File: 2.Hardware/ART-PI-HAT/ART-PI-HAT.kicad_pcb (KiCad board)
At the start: 2 copper layers, 85 x 56 mm, 29 parts, among them J1 Conn_02x20_Odd_Even, J2 Conn_02x20_Odd_Even, J3 GC9A01, U1 XC6206_1.8V, U2 MAX30102, U3 MPU-6050, U4 GP-02, U5 IPEX_CONN

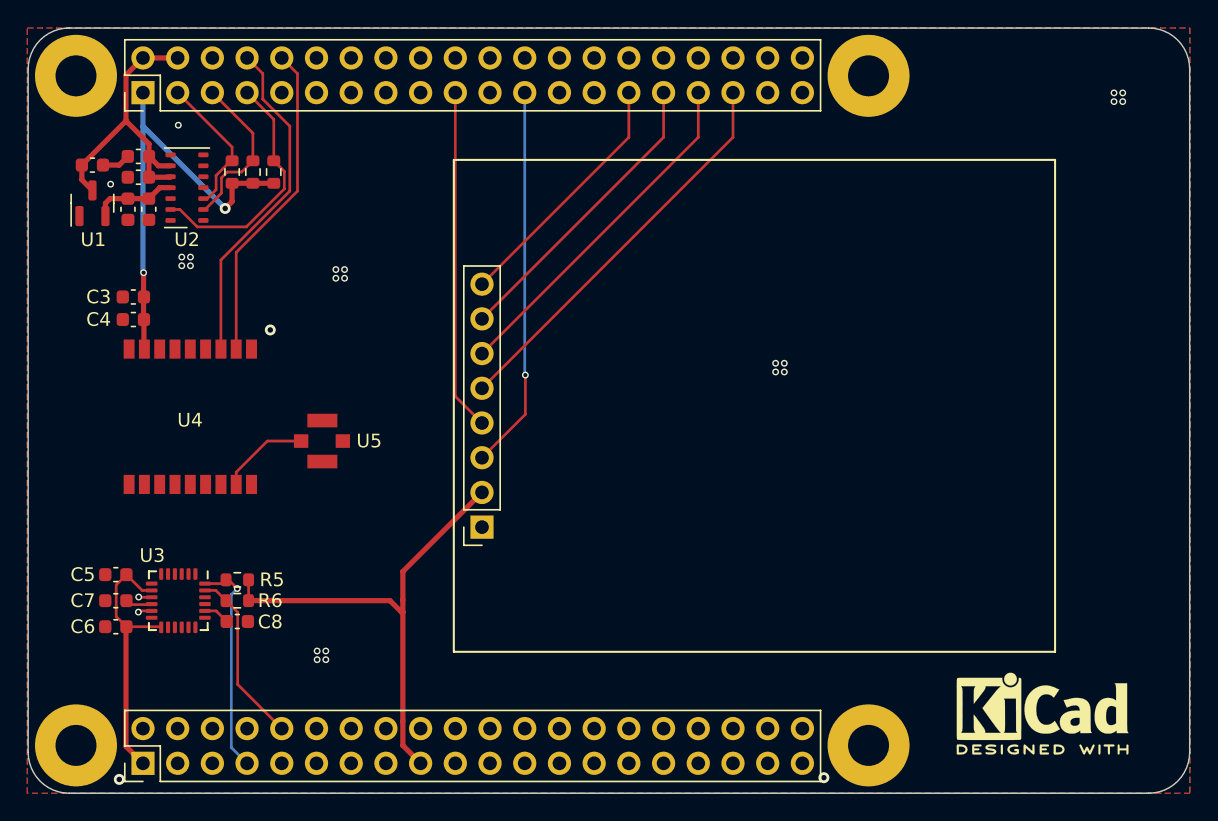
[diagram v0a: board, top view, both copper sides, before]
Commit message: add lever switch.
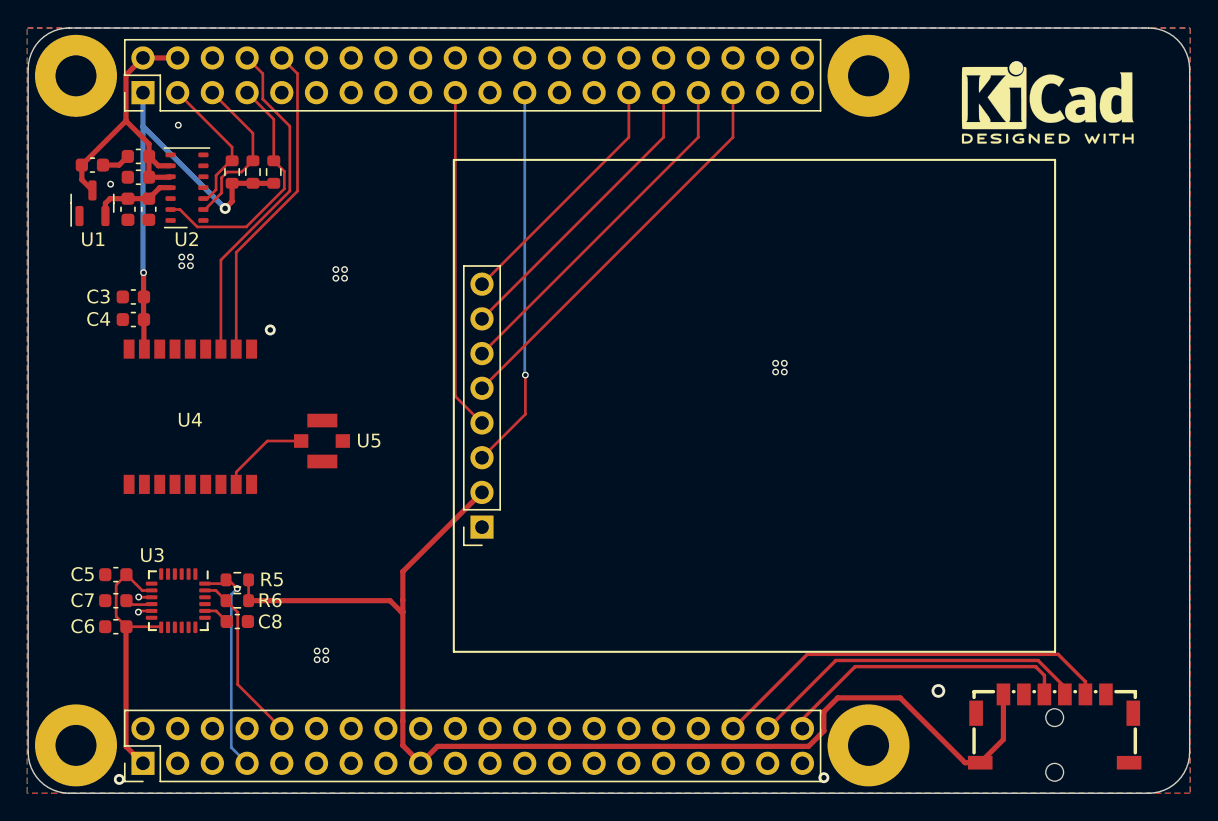
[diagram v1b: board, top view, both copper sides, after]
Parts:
- added SW1: SLLB120300, Library:SW-SMD_SLLB120200, F.Cu at (150.6, 106.8)
- moved REF** 44.7 mm to (150.1, 61.0)
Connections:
- J2 pad 36: unconnected-(J2-Pad36) -> BUTTON_A
- J2 pad 38: unconnected-(J2-Pad38) -> BUTTON_PUSH
- J2 pad 40: unconnected-(J2-Pad40) -> BUTTON_B
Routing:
- net +3V3: track 88.3 -> 139.7 mm
- net BUTTON_A: track 0.00 -> 29.8 mm
- net BUTTON_PUSH: track 0.00 -> 25.2 mm
- net BUTTON_B: track 0.00 -> 21.6 mm
- net GND: vias 28 -> 25

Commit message: update images.
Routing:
- net LCD_SCL: track 28.1 -> 28.0 mm, vias 1 -> 0
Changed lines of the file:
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@@
     )
     (pad_to_mask_clearance 0)
+    (aux_axis_origin 75.438 111.506)
     (pcbplotparams
       (layerselection 0x00010fc_ffffffff)
@@
     (pad "18" smd rect (at 4.7 4.46 270) (size 1.4 0.8) (layers "F.Cu" "F.Paste" "F.Mask")
       (net 82 "unconnected-(U4-Pad18)") (pinfunction "NC") (pintype "no_connect"))
+    (model "${KIPRJMOD}/SIM28ML--3DModel-STEP-56544.STEP"
+      (offset (xyz 0 0 0))
+      (scale (xyz 1 1 1))
+      (rotate (xyz -90 0 0))
+    )
   )
   (footprint "Capacitor_SMD:C_0603_1608Metric" (layer "F.Cu")
@@
       (effects (font (size 1 1) (thickness 0.15)) (justify right))
     )
-    (fp_line (start 2.981 2.7) (end 3.019 2.7) (layer "F.SilkS") (width 0.254))
-    (fp_line (start -5.9 -0.031) (end -5.9 -1.769) (layer "F.SilkS") (width 0.254))
-    (fp_line (start -5.9 2.7) (end -5.9 2.281) (layer "F.SilkS") (width 0.254))
-    (fp_line (start -5.9 2.7) (end -4.481 2.7) (layer "F.SilkS") (width 0.254))
     (fp_line (start 5.9 -0.031) (end 5.9 -1.769) (layer "F.SilkS") (width 0.254))
-    (fp_line (start -0.019 2.7) (end 0.019 2.7) (layer "F.SilkS") (width 0.254))
-    (fp_line (start -3.019 2.7) (end -2.981 2.7) (layer "F.SilkS") (width 0.254))
+    (fp_line (start 1.481 2.7) (end 1.519 2.7) (layer "F.SilkS") (width 0.254))
+    (fp_line (start -5.9 -0.031) (end -5.9 -1.769) (layer "F.SilkS") (width 0.254))
     (fp_line (start 4.481 2.7) (end 5.9 2.7) (layer "F.SilkS") (width 0.254))
-    (fp_line (start -1.519 2.7) (end -1.481 2.7) (layer "F.SilkS") (width 0.254))
+    (fp_line (start -3.019 2.7) (end -2.981 2.7) (layer "F.SilkS") (width 0.254))
+    (fp_line (start -0.019 2.7) (end 0.019 2.7) (layer "F.SilkS") (width 0.254))
+    (fp_line (start -5.9 2.7) (end -5.9 2.281) (layer "F.SilkS") (width 0.254))
     (fp_line (start 5.9 2.7) (end 5.9 2.281) (layer "F.SilkS") (width 0.254))
-    (fp_line (start 1.481 2.7) (end 1.519 2.7) (layer "F.SilkS") (width 0.254))
-    (fp_circle (center 0 -3.2) (end 0.275 -3.2) (layer "Eco2.User") (width 0.55) (fill none))
+    (fp_line (start 2.981 2.7) (end 3.019 2.7) (layer "F.SilkS") (width 0.254))
+    (fp_line (start -1.519 2.7) (end -1.481 2.7) (layer "F.SilkS") (width 0.254))
+    (fp_line (start -5.9 2.7) (end -4.481 2.7) (layer "F.SilkS") (width 0.254))
     (fp_circle (center 0 0.8) (end 0.275 0.8) (layer "Eco2.User") (width 0.55) (fill none))
+    (fp_circle (center 0 -3.2) (end 0.275 -3.2) (layer "Eco2.User") (width 0.55) (fill none))
     (fp_circle (center -6.35 3.3) (end -6.32 3.3) (layer "Eco2.User") (width 0.06) (fill none))
     (fp_poly (pts
-        (xy 1.75 1.7)
-        (xy 2.75 1.7)
-        (xy 2.75 3.3)
-        (xy 1.75 3.3)
+        (xy -6.25 0.2)
+        (xy -5.25 0.2)
+        (xy -5.25 2.05)
+        (xy -6.25 2.05)
       ) (layer "Eco2.User") (width 0.12) (fill solid))
     (fp_poly (pts
@@
       ) (layer "Eco2.User") (width 0.12) (fill solid))
     (fp_poly (pts
-        (xy -2.75 1.7)
-        (xy -1.75 1.7)
-        (xy -1.75 3.3)
-        (xy -2.75 3.3)
+        (xy 4.55 -3)
+        (xy 6.35 -3)
+        (xy 6.35 -2)
+        (xy 4.55 -2)
       ) (layer "Eco2.User") (width 0.12) (fill solid))
     (fp_poly (pts
@@
       ) (layer "Eco2.User") (width 0.12) (fill solid))
     (fp_poly (pts
-        (xy 4.55 -3)
-        (xy 6.35 -3)
-        (xy 6.35 -2)
-        (xy 4.55 -2)
+        (xy 1.75 1.7)
+        (xy 2.75 1.7)
+        (xy 2.75 3.3)
+        (xy 1.75 3.3)
       ) (layer "Eco2.User") (width 0.12) (fill solid))
     (fp_poly (pts
-        (xy 5.25 0.2)
-        (xy 6.25 0.2)
-        (xy 6.25 2.05)
-        (xy 5.25 2.05)
+        (xy -2.75 1.7)
+        (xy -1.75 1.7)
+        (xy -1.75 3.3)
+        (xy -2.75 3.3)
       ) (layer "Eco2.User") (width 0.12) (fill solid))
     (fp_poly (pts
@@
       ) (layer "Eco2.User") (width 0.12) (fill solid))
     (fp_poly (pts
-        (xy -6.25 0.2)
-        (xy -5.25 0.2)
-        (xy -5.25 2.05)
-        (xy -6.25 2.05)
+        (xy 5.25 0.2)
+        (xy 6.25 0.2)
+        (xy 6.25 2.05)
+        (xy 5.25 2.05)
       ) (layer "Eco2.User") (width 0.12) (fill solid))
-    (fp_line (start 6.35 3.3) (end -6.35 3.3) (layer "F.Fab") (width 0.1))
-    (fp_line (start 0.991 -8.647) (end 0.991 -8.342) (layer "F.Fab") (width 0.254))
+    (fp_line (start -1.397 -7.936) (end -1.397 -8.139) (layer "F.Fab") (width 0.254))
+    (fp_line (start -1.295 -8.241) (end -1.092 -8.241) (layer "F.Fab") (width 0.254))
+    (fp_line (start -6.35 -8.977) (end 6.35 -8.977) (layer "F.Fab") (width 0.1))
+    (fp_line (start -4.064 -6.844) (end -4.064 -6.082) (layer "F.Fab") (width 0.254))
     (fp_line (start 1.397 -7.936) (end 1.397 -8.139) (layer "F.Fab") (width 0.254))
-    (fp_line (start 6.35 -8.977) (end 6.35 3.3) (layer "F.Fab") (width 0.1))
-    (fp_line (start 1.092 -8.241) (end 1.295 -8.241) (layer "F.Fab") (width 0.254))
-    (fp_line (start -0.787 -8.85) (end 0.787 -8.85) (layer "F.Fab") (width 0.254))
-    (fp_line (start 4.064 -5.828) (end 4.064 -6.59) (layer "F.Fab") (width 0.254))
     (fp_line (start -6.35 3.3) (end -6.35 -8.977) (layer "F.Fab") (width 0.1))
-    (fp_line (start -6.35 -8.977) (end 6.35 -8.977) (layer "F.Fab") (width 0.1))
+    (fp_line (start 4.064 -5.828) (end 4.064 -6.59) (layer "F.Fab") (width 0.254))
+    (fp_line (start 0.991 -8.647) (end 0.991 -8.342) (layer "F.Fab") (width 0.254))
+    (fp_line (start -0.787 -8.85) (end 0.787 -8.85) (layer "F.Fab") (width 0.254))
+    (fp_line (start 1.092 -8.241) (end 1.295 -8.241) (layer "F.Fab") (width 0.254))
+    (fp_line (start 6.35 3.3) (end -6.35 3.3) (layer "F.Fab") (width 0.1))
+    (fp_line (start 6.35 -8.977) (end 6.35 3.3) (layer "F.Fab") (width 0.1))
     (fp_line (start -0.991 -8.342) (end -0.991 -8.647) (layer "F.Fab") (width 0.254))
-    (fp_line (start -1.295 -8.241) (end -1.092 -8.241) (layer "F.Fab") (width 0.254))
-    (fp_line (start -1.397 -7.936) (end -1.397 -8.139) (layer "F.Fab") (width 0.254))
-    (fp_line (start -4.064 -6.844) (end -4.064 -6.082) (layer "F.Fab") (width 0.254))
-    (fp_arc (start -4.064139 -6.081869) (mid 0.039102 -7.209089) (end 4.064 -5.828) (layer "F.Fab") (width 0.254))
-    (fp_arc (start -1 -8.34) (mid -1.029239 -8.269347) (end -1.099848 -8.24) (layer "F.Fab") (width 0.254))
-    (fp_arc (start 1.1 -8.24) (mid 1.029347 -8.269239) (end 1 -8.339848) (layer "F.Fab") (width 0.254))
-    (fp_arc (start -4.064528 -6.843739) (mid 0.039799 -8.000277) (end 4.064 -6.59) (layer "F.Fab") (width 0.254))
     (fp_arc (start 0.799321 -8.840002) (mid 0.940877 -8.781357) (end 1 -8.64) (layer "F.Fab") (width 0.254))
-    (fp_arc (start -1.000002 -8.639321) (mid -0.941357 -8.780877) (end -0.8 -8.84) (layer "F.Fab") (width 0.254))
-    (fp_arc (start -5.622587 -3.249136) (mid 0.000604 -7.18569) (end 5.623 -3.248) (layer "F.Fab") (width 0.254))
     (fp_arc (start -1.400001 -8.140112) (mid -1.370969 -8.211048) (end -1.3 -8.24) (layer "F.Fab") (width 0.254))
+    (fp_arc (start -5.622587 -3.249136) (mid 0.000604 -7.18569) (end 5.623 -3.248) (layer "F.Fab") (width 0.254))
+    (fp_arc (start -1.000002 -8.639321) (mid -0.941357 -8.780877) (end -0.8 -8.84) (layer "F.Fab") (width 0.254))
     (fp_arc (start 1.300112 -8.240001) (mid 1.371048 -8.210969) (end 1.4 -8.14) (layer "F.Fab") (width 0.254))
+    (fp_arc (start -4.064139 -6.081869) (mid 0.039102 -7.209089) (end 4.064 -5.828) (layer "F.Fab") (width 0.254))
+    (fp_arc (start -1 -8.34) (mid -1.029239 -8.269347) (end -1.099848 -8.24) (layer "F.Fab") (width 0.254))
+    (fp_arc (start -4.064528 -6.843739) (mid 0.039799 -8.000277) (end 4.064 -6.59) (layer "F.Fab") (width 0.254))
+    (fp_arc (start 1.1 -8.24) (mid 1.029347 -8.269239) (end 1 -8.339848) (layer "F.Fab") (width 0.254))
     (pad "" np_thru_hole circle (at 0 -3.2 180) (size 1.3 1.3) (drill 1.3) (layers *.Cu *.Mask))
     (pad "" np_thru_hole circle (at 0 0.8 180) (size 1.3 1.3) (drill 1.3) (layers *.Cu *.Mask))
@@
   (segment (start 94.24652 67.271907) (end 94.24652 65.98952) (width 0.2) (layer "F.Cu") (net 12))
   (segment (start 87.874192 70.05752) (end 91.460907 70.05752) (width 0.2) (layer "F.Cu") (net 12))
-  (segment (start 106.76 82.454) (end 106.76 60.23) (width 0.2) (layer "F.Cu") (net 15))
-  (segment (start 108.712 84.406) (end 106.76 82.454) (width 0.2) (layer "F.Cu") (net 15))
-  (segment (start 111.887 83.771) (end 108.712 86.946) (width 0.2) (layer "F.Cu") (net 17))
-  (segment (start 111.887 80.899) (end 111.887 83.771) (width 0.2) (layer "F.Cu") (net 17))
-  (via (at 111.887 80.899) (size 0.5) (drill 0.3) (layers "F.Cu" "B.Cu") (net 17))
-  (segment (start 111.887 80.899) (end 111.84 80.852) (width 0.2) (layer "B.Cu") (net 17))
-  (segment (start 111.84 80.852) (end 111.84 60.23) (width 0.2) (layer "B.Cu") (net 17))
+  (segment (start 106.76 82.454) (end 106.76 60.23) (width 0.2) (layer "B.Cu") (net 15))
+  (segment (start 108.712 84.406) (end 106.76 82.454) (width 0.2) (layer "B.Cu") (net 15))
+  (segment (start 111.84 60.23) (end 111.84 83.818) (width 0.2) (layer "B.Cu") (net 17))
+  (segment (start 111.84 83.818) (end 108.712 86.946) (width 0.2) (layer "B.Cu") (net 17))
   (segment (start 108.712 81.866) (end 127.08 63.498) (width 0.2) (layer "F.Cu") (net 18))
   (segment (start 127.08 63.498) (end 127.08 60.23) (width 0.2) (layer "F.Cu") (net 18))
